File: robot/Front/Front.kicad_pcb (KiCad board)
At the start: 2 copper layers, 40 x 40 mm, 41 parts, among them J1 USB_B_Micro, Q1 BC849, Q2 BC849, SW2 SW_Push, U1 CH340C, U10 ESP32-WROOM-32, U2 CJVL53L0XV2, U3 SPX3819M5-L-3-3

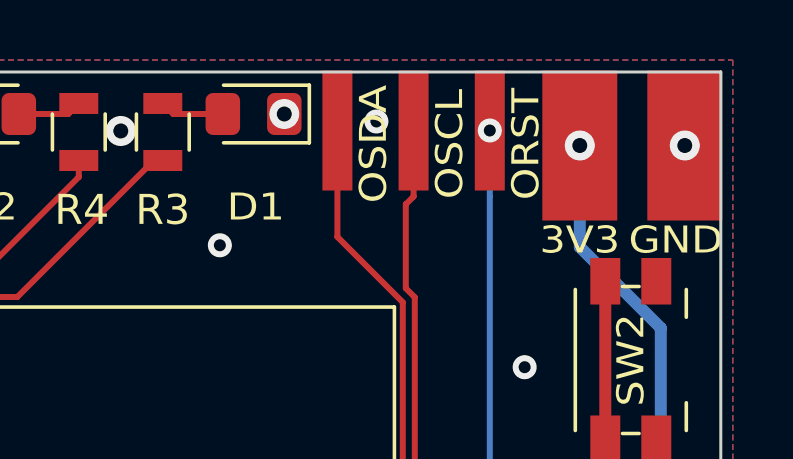
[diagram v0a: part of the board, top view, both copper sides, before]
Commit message: Finish Top, remap OLED pins
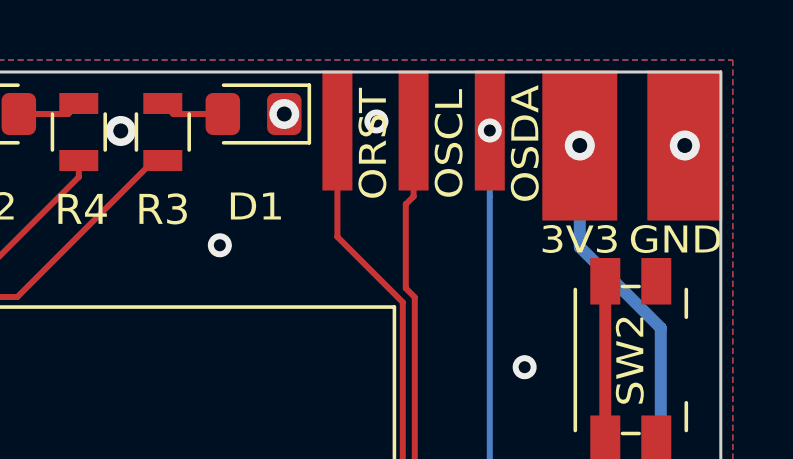
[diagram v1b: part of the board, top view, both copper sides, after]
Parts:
- moved H14 5.08 mm to (227.8, 105.0)
- moved H16 5.08 mm to (222.7, 105.0)
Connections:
- U10 pad 33: /OLED_SDA -> /OLED_~RES
- U10 pad 37: /OLED_~RES -> /OLED_SDA
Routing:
- net /OLED_SDA: track 26.2 -> 16.7 mm, vias 0 -> 2
- net /OLED_~RES: track 16.7 -> 26.2 mm, vias 2 -> 0

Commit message: Small fixes, step files
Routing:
- net +3V3: track 99.3 -> 96.1 mm, vias 6 -> 8
- net /D+: track 20.5 -> 22.6 mm
- net /D-: track 23.2 -> 24.6 mm
- net /GPIO0: track 31.0 -> 30.0 mm
- net /RXD-TXD: track 27.9 -> 28.9 mm
- net /~RST: track 49.8 -> 50.4 mm
- net /TXD-RXD: track 26.6 -> 26.1 mm
- net /OLED_SDA: track 16.7 -> 17.0 mm, vias 2 -> 0
- net GND: vias 47 -> 36

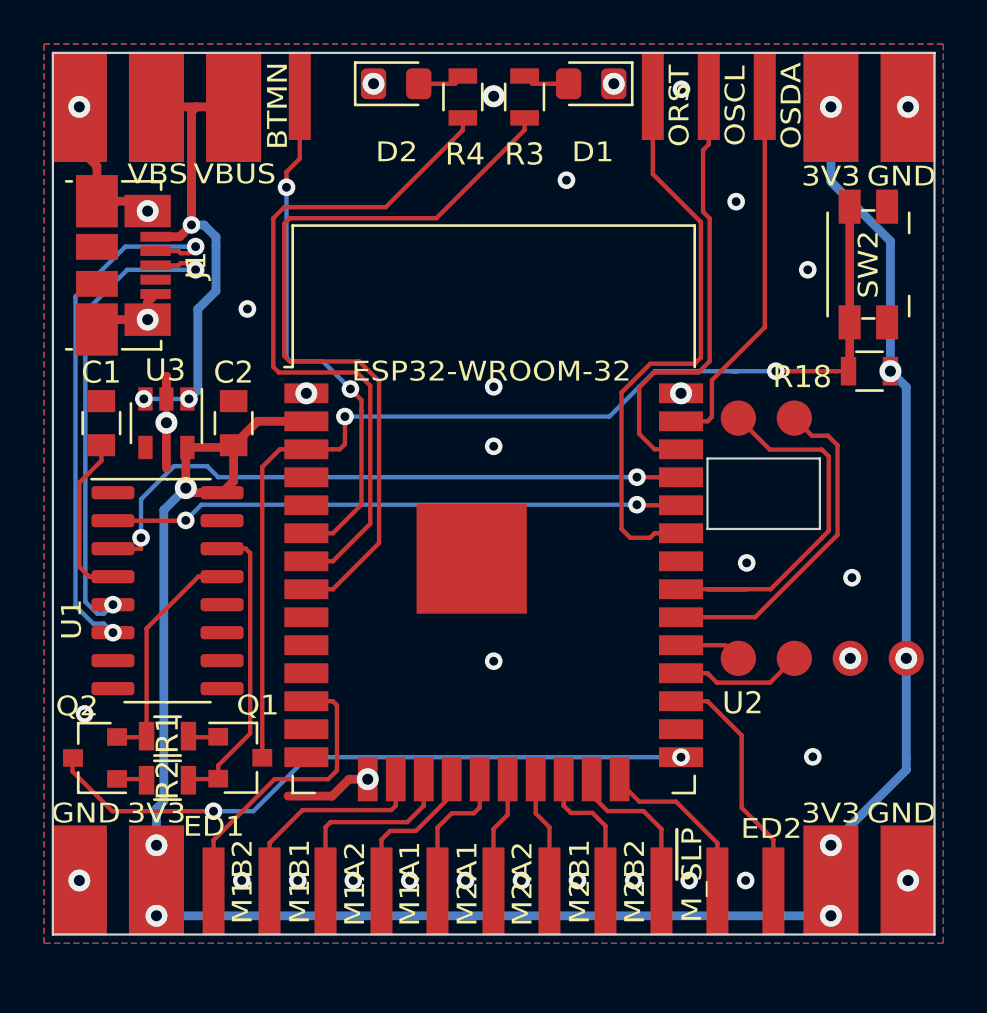
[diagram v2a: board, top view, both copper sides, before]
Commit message: Layout changes, new footprints, added Side PCB
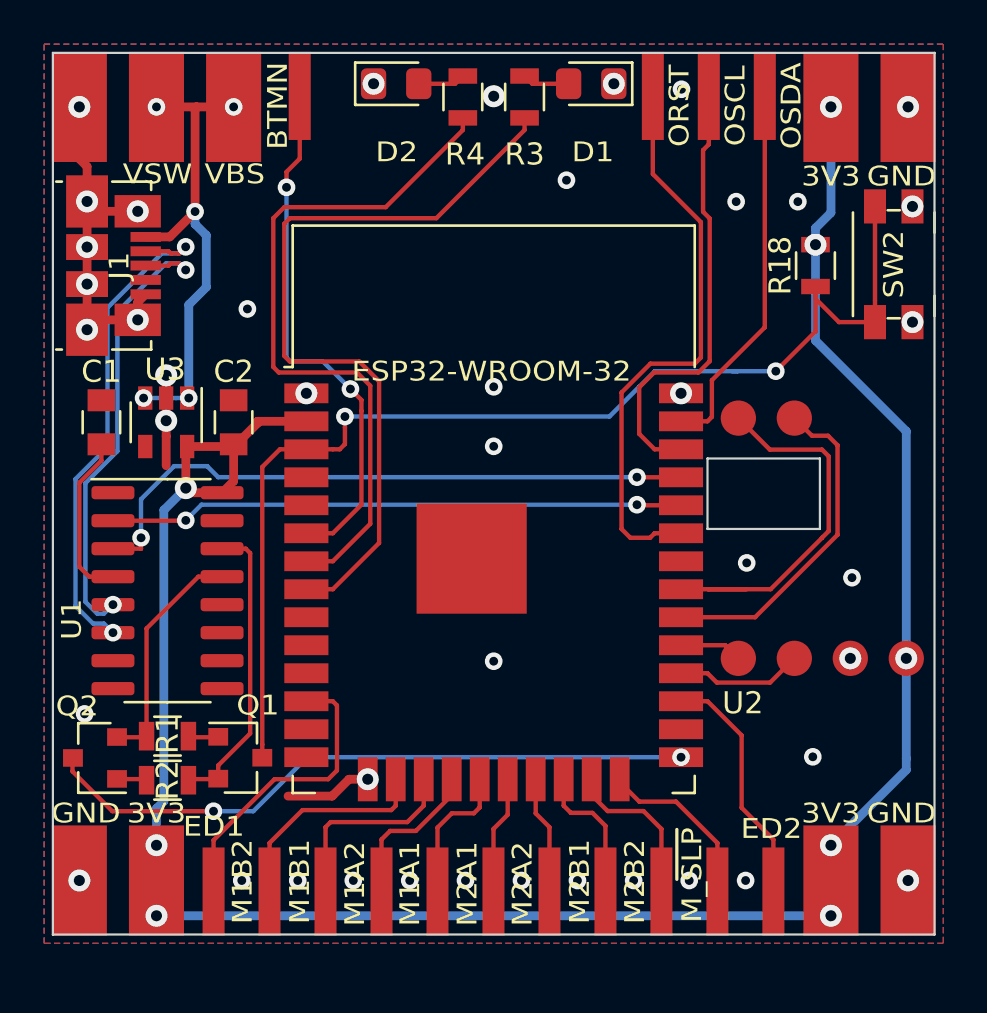
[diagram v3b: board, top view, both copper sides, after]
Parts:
- H1: value VBUS -> VBS
- H17: value VBS -> VSW
- J1: footprint Connectors_USB:USB_Micro-B_Molex_47346-0001 -> Connector_USB:USB_Micro-B_Molex_47346-0001
- moved R18 5.38 mm to (230.1, 112.7), turned to 270 degrees
- moved SW2 1.15 mm to (233.7, 112.6)
- moved J1 0.75 mm to (198.2, 112.7)
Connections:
- J1 pad 4: (no net) -> Net-(J1-Pad4)
- U1 pad 10: (no net) -> Net-(U1-Pad10)
- U1 pad 11: (no net) -> Net-(U1-Pad11)
- U1 pad 12: (no net) -> Net-(U1-Pad12)
- U1 pad 15: (no net) -> Net-(U1-Pad15)
- U1 pad 7: (no net) -> Net-(U1-Pad7)
- U1 pad 8: (no net) -> Net-(U1-Pad8)
- U1 pad 9: (no net) -> Net-(U1-Pad9)
- U10 pad 10: (no net) -> Net-(U10-Pad10)
- U10 pad 11: (no net) -> Net-(U10-Pad11)
- U10 pad 13: (no net) -> Net-(U10-Pad13)
- U10 pad 14: (no net) -> Net-(U10-Pad14)
- U10 pad 26: (no net) -> Net-(U10-Pad26)
- U10 pad 32: (no net) -> Net-(U10-Pad32)
- U10 pad 4: (no net) -> Net-(U10-Pad4)
- U10 pad 5: (no net) -> Net-(U10-Pad5)
- U10 pad 9: (no net) -> Net-(U10-Pad9)
- U3 pad 4: (no net) -> Net-(U3-Pad4)
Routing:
- net GND: track 21.3 -> 27.1 mm, vias 36 -> 43
- net /~RST: track 50.4 -> 52.8 mm
- net /D-: track 24.6 -> 23.0 mm
- net VBUS: track 26.3 -> 24.8 mm, vias 3 -> 5
- net /D+: track 22.6 -> 21.5 mm
- net +3V3: track 96.1 -> 96.7 mm

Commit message: Changes to structure
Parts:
- C1, C2: footprint Capacitors_SMD:C_0805 -> Capacitor_SMD:C_0805_2012Metric
- R1, R18, R2, R3, R4: footprint Resistors_SMD:R_0805 -> Resistor_SMD:R_0805_2012Metric
- moved J1 0.45 mm to (197.8, 112.7)

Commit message: Small changes, connectors
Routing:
- net VBUS: track 24.4 -> 21.9 mm
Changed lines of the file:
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@@
     (thickness 1.6)
     (drawings 8)
-    (tracks 381)
+    (tracks 379)
     (zones 0)
     (modules 41)
@@
   (segment (start 197.7 121.5) (end 196.7 122.5) (width 0.2) (layer F.Cu) (net 2))
   (segment (start 197.7 121.5) (end 197.7 120.76) (width 0.2) (layer F.Cu) (net 2))
-  (segment (start 200.2 105.45) (end 200.2 106.7) (width 0.4) (layer F.Cu) (net 3) (status 30))
-  (segment (start 203.7 105.45) (end 203.7 106.7) (width 0.4) (layer F.Cu) (net 3) (status 30))
   (segment (start 201.6 118.7) (end 201.675002 118.7) (width 0.2) (layer F.Cu) (net 3) (status 30))
   (segment (start 199.7 118.7) (end 199.624998 118.7) (width 0.2) (layer F.Cu) (net 3) (status 30))

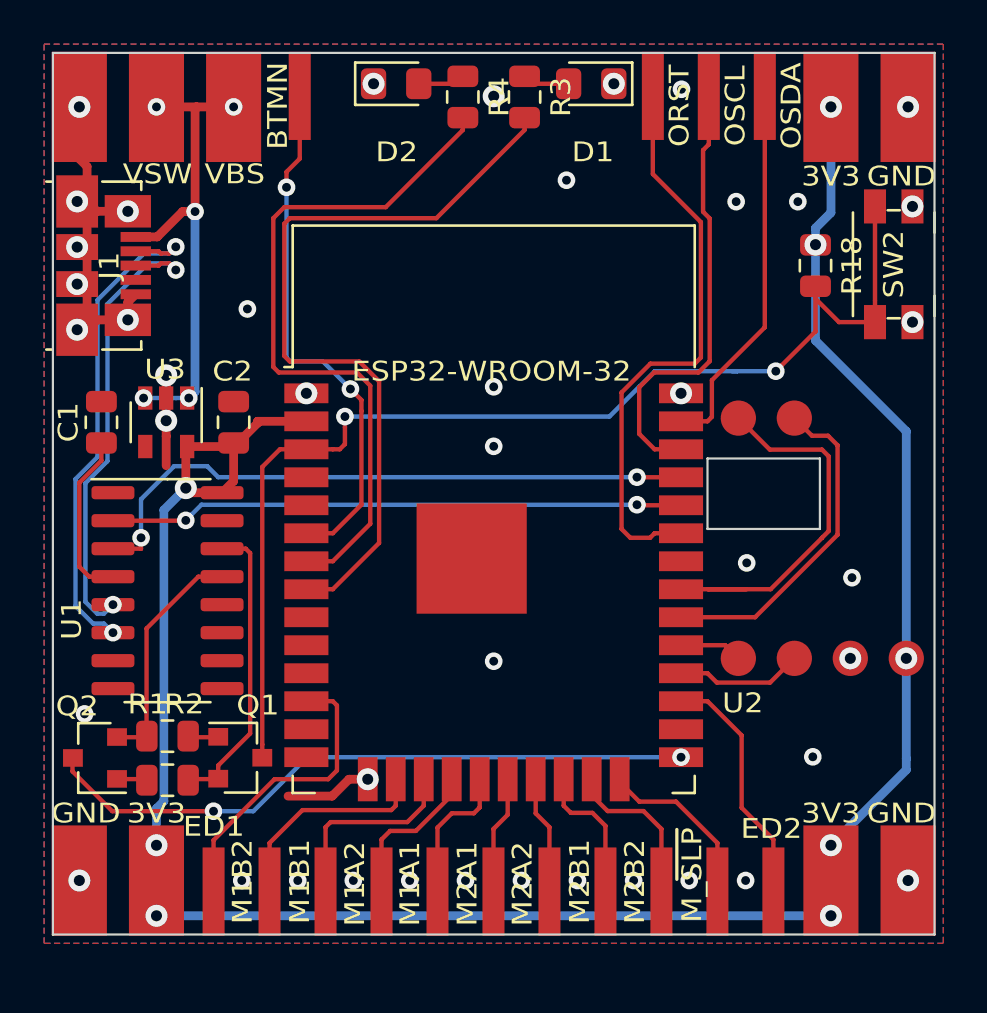
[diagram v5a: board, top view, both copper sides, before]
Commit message: Add VBS, Add Silk deco, small changes
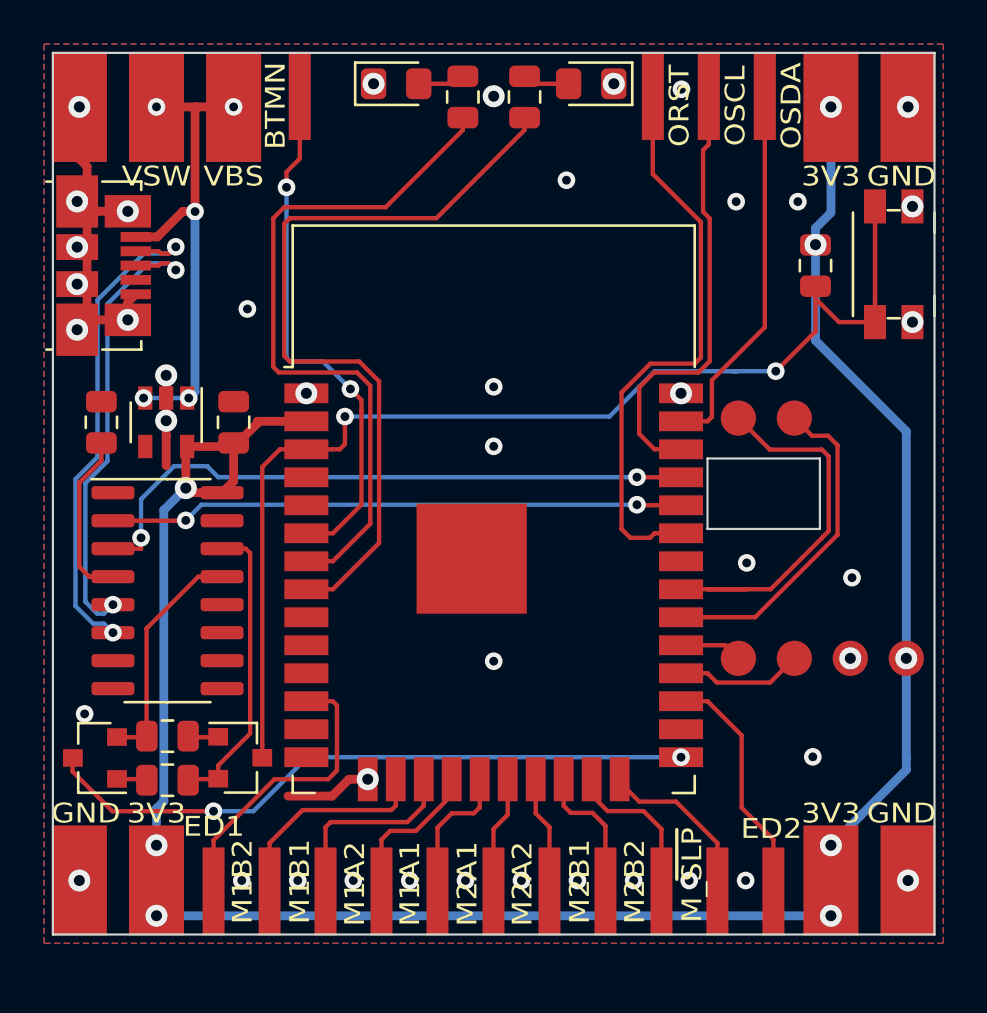
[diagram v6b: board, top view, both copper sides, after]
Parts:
- added G***: LOGO, Print:d1, B.Cu at (215.5, 123.0)

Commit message: Small changes, BOM, Gerbers
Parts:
- H1: value VBS -> VBUS
- H17: value VSW -> VBS
- H2: value M_~SLP -> M~SLP
- moved G*** 0.10 mm to (215.6, 123.0)
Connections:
- J1 pad 4: Net-(J1-Pad4) -> (no net)
- U1 pad 10: Net-(U1-Pad10) -> (no net)
- U1 pad 11: Net-(U1-Pad11) -> (no net)
- U1 pad 12: Net-(U1-Pad12) -> (no net)
- U1 pad 15: Net-(U1-Pad15) -> (no net)
- U1 pad 7: Net-(U1-Pad7) -> (no net)
- U1 pad 8: Net-(U1-Pad8) -> (no net)
- U1 pad 9: Net-(U1-Pad9) -> (no net)
- U10 pad 10: Net-(U10-Pad10) -> (no net)
- U10 pad 11: Net-(U10-Pad11) -> (no net)
- U10 pad 13: Net-(U10-Pad13) -> (no net)
- U10 pad 14: Net-(U10-Pad14) -> (no net)
- U10 pad 26: Net-(U10-Pad26) -> (no net)
- U10 pad 32: Net-(U10-Pad32) -> (no net)
- U10 pad 4: Net-(U10-Pad4) -> (no net)
- U10 pad 5: Net-(U10-Pad5) -> (no net)
- U10 pad 9: Net-(U10-Pad9) -> (no net)
- U3 pad 4: Net-(U3-Pad4) -> (no net)
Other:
- board text added: "Cuby V0.1"
